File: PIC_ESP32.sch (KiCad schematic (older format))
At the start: 54 parts, among them J1 USB_B_Micro, J2 12V_SMPS, J3 12V_BATT, J4 BME, J5 LCD, J6 FANS, J7 IR sensor, SW1 EN, SW2 SW_Reed, SW3 FLASH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

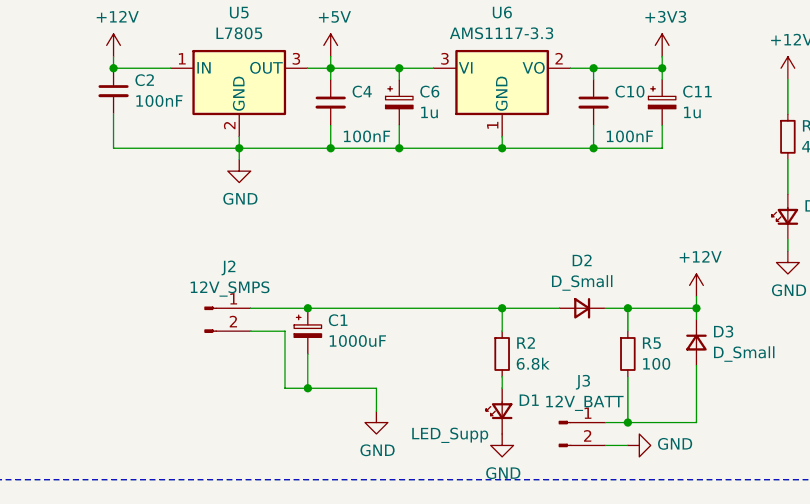
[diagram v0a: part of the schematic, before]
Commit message: added fuse
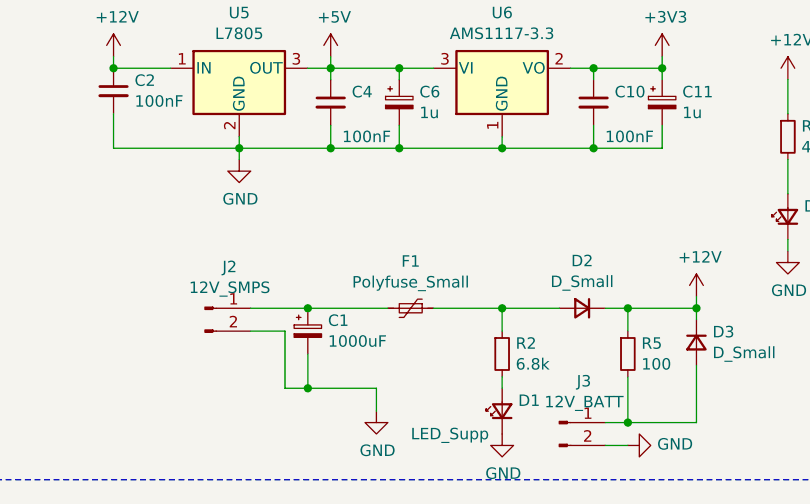
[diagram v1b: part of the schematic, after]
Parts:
- added F1: Polyfuse_Small, symbol Device:Polyfuse_Small
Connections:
- net at D2.2 (A), R2.1: now also F1.1; no longer C1.1, J2.1 (Pin_1)
- new net: C1.1, F1.2, J2.1 (Pin_1)
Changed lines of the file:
@@
 Connection ~ 2300 6900
 Wire Wire Line
-	2300 6900 3150 6900
+	2300 6900 2650 6900
 Wire Wire Line
 	3150 6900 3400 6900
@@
 	9600 3050 9750 3050
 NoConn ~ 9750 3550
+$Comp
+L Device:Polyfuse_Small F1
+U 1 1 608CC477
+P 2750 6900
+F 0 "F1" V 2545 6900 50  0000 C CNN
+F 1 "Polyfuse_Small" V 2636 6900 50  0000 C CNN
+F 2 "" H 2800 6700 50  0001 L CNN
+F 3 "~" H 2750 6900 50  0001 C CNN
+	1    2750 6900
+	0    1    1    0
+$EndComp
+Wire Wire Line
+	2850 6900 3150 6900
 $EndSCHEMATC
